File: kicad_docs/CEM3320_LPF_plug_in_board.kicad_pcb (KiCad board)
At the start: 2 copper layers, 58.4 x 50.8 mm, 42 parts, among them J1 signal_in, J2 signal_in, J3 signal_out, J4 Conn_01x08_Male, U1 CEM3320, U2 TL072

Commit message: add rendered pics of board top and bottom
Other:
- board text added: "github.com/JordanAceto/CEM3320_LPF_plug_in_board rev1.0 2019-06-09"
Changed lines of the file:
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@@
   (general
     (thickness 1.6)
-    (drawings 9)
+    (drawings 10)
     (tracks 223)
     (zones 0)
@@
     )
   )
+  (gr_text "github.com/JordanAceto/CEM3320_LPF_plug_in_board\nrev1.0\n2019-06-09" (at 177.292 79.629) (layer B.SilkS)
+    (effects (font (size 1 1) (thickness 0.15)) (justify left mirror))
+  )
   (gr_text feedback (at 177.038 116.586) (layer F.SilkS)

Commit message: fix silkscreen issue where R8 and R6 refs overlapped
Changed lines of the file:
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@@
     (pcbplotparams
       (layerselection 0x010fc_ffffffff)
-      (usegerberextensions false)
+      (usegerberextensions true)
       (usegerberattributes false)
       (usegerberadvancedattributes false)
@@
       (psa4output false)
       (plotreference true)
-      (plotvalue true)
+      (plotvalue false)
       (plotinvisibletext false)
       (padsonsilk false)
@@
       (outputformat 1)
       (mirror false)
-      (drillshape 1)
+      (drillshape 0)
       (scaleselection 1)
-      (outputdirectory ""))
+      (outputdirectory "gerbers/"))
   )
   (net 0 "")
@@
     (tags "resistor handsolder")
     (attr smd)
-    (fp_text reference R8 (at 0 -1.65) (layer F.SilkS)
-      (effects (font (size 1 1) (thickness 0.15)))
-    )
+    (fp_text reference R8 (at 0 1.778) (layer F.SilkS)
+      (effects (font (size 1 1) (thickness 0.15)))
+    )

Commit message: fix reversed power pins on TL072 in schm and brd, delete bad gerbers
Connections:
- U2 pad 4: +12V -> -12V
- U2 pad 8: -12V -> +12V
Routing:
- net +12V: track 103.6 -> 87.3 mm, vias 1 -> 2
- net -12V: track 154.0 -> 149.4 mm
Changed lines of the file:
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@@
     (thickness 1.6)
     (drawings 10)
-    (tracks 223)
+    (tracks 225)
     (zones 0)
     (modules 42)
@@
   )
   (setup
-    (last_trace_width 0.25)
+    (last_trace_width 0.762)
     (user_trace_width 0.762)
     (trace_clearance 0.2)
@@
     (fp_line (start 0 2.56) (end 1.95 2.56) (layer F.SilkS) (width 0.12))
     (pad 8 smd roundrect (at 2.475 -1.905) (size 1.95 0.6) (layers F.Cu F.Paste F.Mask) (roundrect_rratio 0.25)
-      (net 4 -12V))
+      (net 3 +12V))
     (pad 7 smd roundrect (at 2.475 -0.635) (size 1.95 0.6) (layers F.Cu F.Paste F.Mask) (roundrect_rratio 0.25)
       (net 30 "Net-(C12-Pad1)"))
@@
       (net 27 "Net-(R19-Pad1)"))
     (pad 4 smd roundrect (at -2.475 1.905) (size 1.95 0.6) (layers F.Cu F.Paste F.Mask) (roundrect_rratio 0.25)
-      (net 3 +12V))
+      (net 4 -12V))
     (pad 3 smd roundrect (at -2.475 0.635) (size 1.95 0.6) (layers F.Cu F.Paste F.Mask) (roundrect_rratio 0.25)
       (net 1 GND))
@@
   (segment (start 157.988 97.16663) (end 157.988 95.758) (width 0.25) (layer F.Cu) (net 2))
   (segment (start 157.988 98.298) (end 157.988 97.16663) (width 0.25) (layer F.Cu) (net 2))
-  (via (at 158.242 118.11) (size 0.8) (drill 0.4) (layers F.Cu B.Cu) (net 3))
-  (segment (start 182.88 121.92) (end 162.052 121.92) (width 0.762) (layer B.Cu) (net 3))
-  (segment (start 162.052 121.92) (end 158.242 118.11) (width 0.762) (layer B.Cu) (net 3))
-  (segment (start 158.242 116.778) (end 158.307 116.713) (width 0.762) (layer F.Cu) (net 3))
-  (segment (start 158.242 118.11) (end 158.242 116.778) (width 0.762) (layer F.Cu) (net 3))
   (segment (start 173.228 96.012) (end 170.434 93.218) (width 0.762) (layer B.Cu) (net 3))
   (segment (start 161.909001 84.216999) (end 158.787999 87.338001) (width 0.762) (layer B.Cu) (net 3))
-  (segment (start 173.228 112.268) (end 173.228 96.012) (width 0.762) (layer B.Cu) (net 3))
   (segment (start 158.787999 87.338001) (end 157.988 88.138) (width 0.762) (layer B.Cu) (net 3))
   (segment (start 182.88 121.92) (end 173.228 112.268) (width 0.762) (layer B.Cu) (net 3))
@@
   (segment (start 157.988 88.138) (end 159.004 87.122) (width 0.25) (layer F.Cu) (net 3))
   (segment (start 159.004 87.122) (end 159.004 85.04381) (width 0.25) (layer F.Cu) (net 3))
+  (segment (start 163.257 112.903) (end 163.257 111.571) (width 0.762) (layer F.Cu) (net 3))
+  (via (at 164.592 111.506) (size 0.8) (drill 0.4) (layers F.Cu B.Cu) (net 3))
+  (segment (start 163.257 111.571) (end 163.322 111.506) (width 0.762) (layer F.Cu) (net 3))
+  (segment (start 163.322 111.506) (end 164.592 111.506) (width 0.762) (layer F.Cu) (net 3))
+  (segment (start 164.592 111.506) (end 173.228 111.506) (width 0.762) (layer B.Cu) (net 3))
+  (segment (start 173.228 112.268) (end 173.228 111.506) (width 0.762) (layer B.Cu) (net 3))
+  (segment (start 173.228 111.506) (end 173.228 96.012) (width 0.762) (layer B.Cu) (net 3))
+  (segment (start 163.322 111.506) (end 163.322 111.506) (width 0.762) (layer F.Cu) (net 3))
+  (via (at 163.322 111.506) (size 0.8) (drill 0.4) (layers F.Cu B.Cu) (net 3))
   (segment (start 148.844 82.287) (end 148.853 82.296) (width 0.25) (layer F.Cu) (net 4))
   (segment (start 148.844 78.994) (end 148.844 82.287) (width 0.25) (layer F.Cu) (net 4))
@@
   (segment (start 174.53499 94.45101) (end 174.53499 92.456) (width 0.25) (layer F.Cu) (net 4))
   (segment (start 173.482 95.504) (end 174.53499 94.45101) (width 0.25) (layer F.Cu) (net 4))
-  (segment (start 162.182 112.903) (end 163.257 112.903) (width 0.762) (layer F.Cu) (net 4))
-  (segment (start 182.88 119.38) (end 182.88 119.634) (width 0.762) (layer F.Cu) (net 4))
-  (segment (start 162.854886 122.936) (end 161.70099 121.782104) (width 0.762) (layer F.Cu) (net 4))
-  (segment (start 182.88 119.634) (end 179.578 122.936) (width 0.762) (layer F.Cu) (net 4))
-  (segment (start 161.70099 113.38401) (end 162.182 112.903) (width 0.762) (layer F.Cu) (net 4))
-  (segment (start 179.578 122.936) (end 162.854886 122.936) (width 0.762) (layer F.Cu) (net 4))
-  (segment (start 161.70099 121.782104) (end 161.70099 113.38401) (width 0.762) (layer F.Cu) (net 4))
   (segment (start 181.864 120.396) (end 182.88 119.38) (width 0.762) (layer F.Cu) (net 4))
   (segment (start 179.832 120.396) (end 181.864 120.396) (width 0.762) (layer F.Cu) (net 4))
@@
   (segment (start 164.32899 96.81826) (end 164.32899 93.22701) (width 0.25) (layer F.Cu) (net 4))
   (segment (start 154.178 104.902) (end 157.48 101.6) (width 0.25) (layer F.Cu) (net 4))
+  (segment (start 143.597 121.795) (end 142.24 121.795) (width 0.762) (layer F.Cu) (net 4))
+  (segment (start 158.422999 123.771001) (end 145.573001 123.771001) (width 0.762) (layer F.Cu) (net 4))
   (segment (start 145.573001 123.771001) (end 143.597 121.795) (width 0.762) (layer F.Cu) (net 4))
-  (segment (start 143.597 121.795) (end 142.24 121.795) (width 0.762) (layer F.Cu) (net 4))
-  (segment (start 162.019885 123.771001) (end 145.573001 123.771001) (width 0.762) (layer F.Cu) (net 4))
-  (segment (start 162.854886 122.936) (end 162.019885 123.771001) (width 0.762) (layer F.Cu) (net 4))
+  (segment (start 158.307 123.655002) (end 158.422999 123.771001) (width 0.762) (layer F.Cu) (net 4))
+  (segment (start 158.307 116.713) (end 158.307 123.655002) (width 0.762) (layer F.Cu) (net 4))
+  (segment (start 179.578 122.936) (end 182.88 119.634) (width 0.762) (layer F.Cu) (net 4))
+  (segment (start 158.422999 123.771001) (end 174.551999 123.771001) (width 0.762) (layer F.Cu) (net 4))
+  (segment (start 182.88 119.634) (end 182.88 119.38) (width 0.762) (layer F.Cu) (net 4))
+  (segment (start 175.387 122.936) (end 179.578 122.936) (width 0.762) (layer F.Cu) (net 4))
+  (segment (start 174.551999 123.771001) (end 175.387 122.936) (width 0.762) (layer F.Cu) (net 4))
   (segment (start 153.707999 97.498001) (end 155.448 95.758) (width 0.25) (layer F.Cu) (net 5))
   (segment (start 152.908 98.298) (end 153.707999 97.498001) (width 0.25) (layer F.Cu) (net 5))

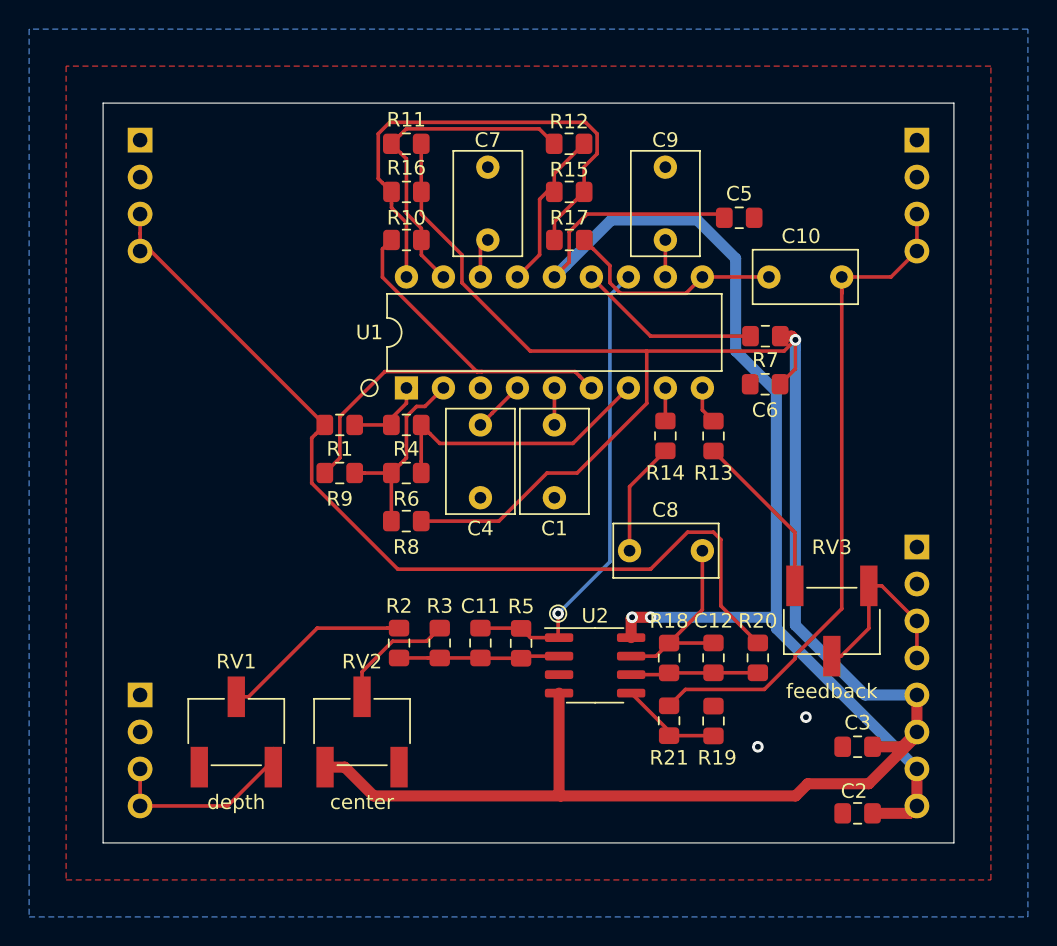
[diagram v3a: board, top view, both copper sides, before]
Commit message: update pcb silkscreen
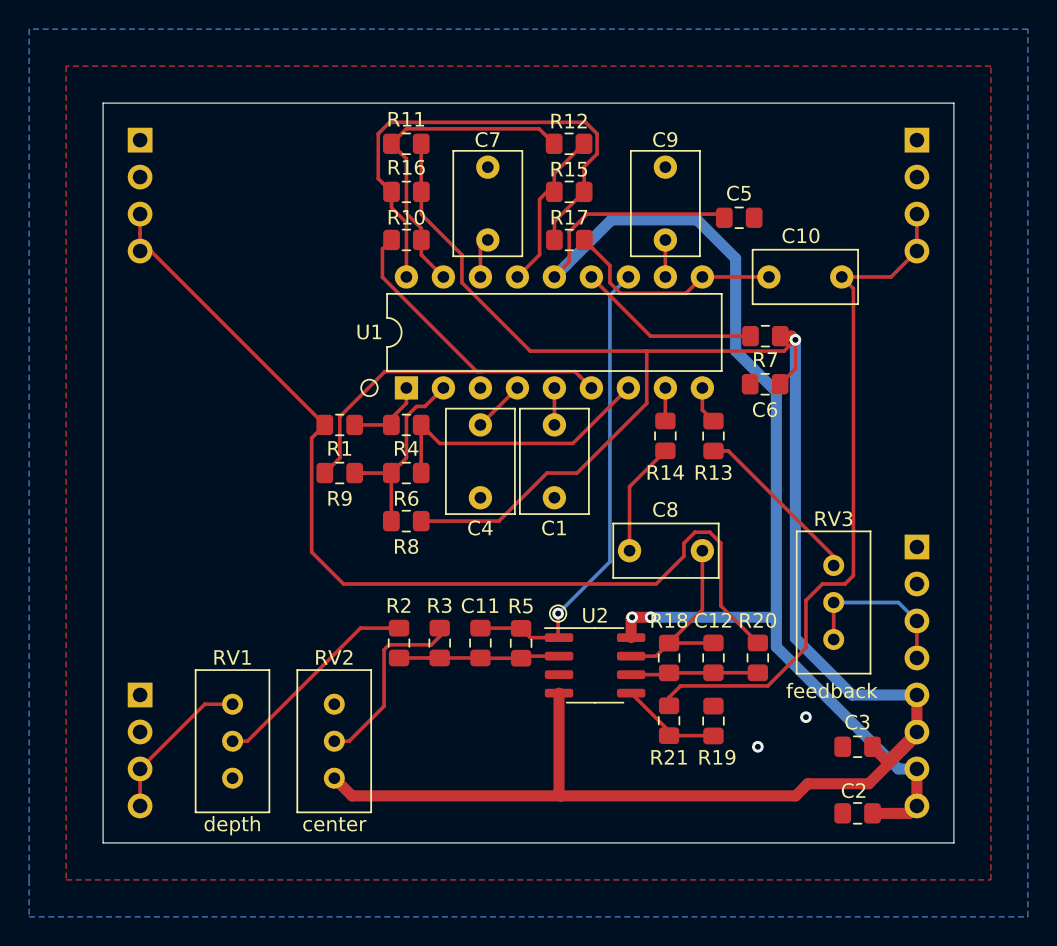
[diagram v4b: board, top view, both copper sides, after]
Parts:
- RV1, RV2, RV3: footprint Potentiometer_SMD:Potentiometer_Bourns_3269W_Vertical -> Potentiometer_THT:Potentiometer_Bourns_3296W_Vertical
- moved RV2 3.70 mm to (142.9, 122.6), turned to 270 degrees
- moved RV1 3.19 mm to (135.9, 122.6), turned to 270 degrees
- moved RV3 1.28 mm to (177.2, 113.0), turned to 270 degrees
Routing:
- net Net-(R3-Pad1): track 8.29 -> 13.1 mm
- net /dry: track 64.5 -> 68.5 mm
- net Net-(J1-Pad3): track 13.8 -> 10.7 mm
- net Net-(J4-Pad3): track 13.1 -> 11.3 mm
- net Net-(R2-Pad2): track 13.1 -> 14.6 mm
- net /wet: track 47.1 -> 47.9 mm
- net +12V: track 87.3 -> 88.0 mm
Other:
- board text added: "+12V"
- board text added: "-12V"
- board text added: "cv in"
- board text added: "github.com/JordanAceto/CEM3320_LPF_plug_in_board rev1.1 2020-02-02"
- board text added: "gnd"
- board text added: "rez cv in"
- board text added: "signal in"
- board text added: "signal out"
- board text removed: "github.com/JordanAceto/CEM3320_LPF_plug_in_board rev1.0 2019-06-09"
